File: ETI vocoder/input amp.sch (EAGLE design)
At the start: 32 parts, among them IC1 LM4558N, IC2 LM1458N

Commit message: Fixed input boards in regards to article and added spacer holes
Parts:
- C4: device resistor:C-EU050-025X075 -> resistor:C-EU025-025X050
- R8: value (none) -> 47k
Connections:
- net N$10: now also RV2G$1.1E; no longer RV2G$1.1A
- net N$9: now also RV2G$1.1A; no longer RV2G$1.1E
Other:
- note added: "Har sjekket footprint caps"
- note added: "Har sjekket retning på pots!"
- note removed: "Sjekk retning på pots!"
- moved on the sheet: RV2
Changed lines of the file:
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@@
 <?xml version="1.0" encoding="utf-8"?>
 <!DOCTYPE eagle SYSTEM "eagle.dtd">
-<eagle version="7.2.0">
+<eagle version="6.2">
 <drawing>
 <settings>
@@
 <layers>
 <layer number="1" name="Top" color="4" fill="1" visible="no" active="no"/>
+<layer number="2" name="Route2" color="1" fill="3" visible="no" active="no"/>
+<layer number="3" name="Route3" color="4" fill="3" visible="no" active="no"/>
+<layer number="14" name="Route14" color="1" fill="6" visible="no" active="no"/>
+<layer number="15" name="Route15" color="4" fill="6" visible="no" active="no"/>
 <layer number="16" name="Bottom" color="1" fill="1" visible="no" active="no"/>
 <layer number="17" name="Pads" color="2" fill="1" visible="no" active="no"/>
@@
 <part name="R6" library="resistor" deviceset="R-EU_" device="0207/7" value="1k5"/>
 <part name="R7" library="resistor" deviceset="R-EU_" device="0207/7" value="51k"/>
-<part name="R8" library="resistor" deviceset="R-EU_" device="0207/7"/>
+<part name="R8" library="resistor" deviceset="R-EU_" device="0207/7" value="47k"/>
 <part name="R9" library="resistor" deviceset="R-EU_" device="0207/7" value="51k"/>
 <part name="R10" library="resistor" deviceset="R-EU_" device="0207/7" value="47k"/>
@@
 <part name="C2" library="resistor" deviceset="CPOL-EU" device="E2.5-5" value="22u"/>
 <part name="C3" library="resistor" deviceset="C-EU" device="050-025X075" value="220n"/>
-<part name="C4" library="resistor" deviceset="C-EU" device="050-025X075" value="68p"/>
+<part name="C4" library="resistor" deviceset="C-EU" device="025-025X050" value="68p"/>
 <part name="C5" library="resistor" deviceset="C-EU" device="050-025X075" value="2n2"/>
 <part name="C6" library="resistor" deviceset="C-EU" device="050-025X075" value="2n2"/>
@@
 <sheet>
 <plain>
-<text x="-12.7" y="101.6" size="1.778" layer="91">Sjekk retning på pots!</text>
+<text x="-12.7" y="101.6" size="1.778" layer="91">Har sjekket retning på pots!</text>
+<text x="-12.7" y="96.52" size="1.778" layer="91">Har sjekket footprint caps</text>
 </plain>
 <instances>
@@
 </instance>
 <instance part="GND3" gate="1" x="66.04" y="50.8"/>
-<instance part="RV2" gate="G$1" x="88.9" y="63.5" smashed="yes" rot="R90">
-<attribute name="NAME" x="85.344" y="59.436" size="1.778" layer="95" rot="R90"/>
+<instance part="RV2" gate="G$1" x="88.9" y="63.5" smashed="yes" rot="MR270">
+<attribute name="NAME" x="85.344" y="67.564" size="1.778" layer="95" rot="MR270"/>
 </instance>
 <instance part="GND4" gate="1" x="101.6" y="55.88"/>
@@
 <label x="66.04" y="33.02" size="1.778" layer="95"/>
 <junction x="66.04" y="22.86"/>
+<junction x="66.04" y="33.02"/>
 </segment>
 <segment>
@@
 <wire x1="73.66" y1="71.12" x2="96.52" y2="71.12" width="0.1524" layer="91"/>
 <wire x1="96.52" y1="71.12" x2="96.52" y2="68.58" width="0.1524" layer="91"/>
-<pinref part="RV2" gate="G$1" pin="1E"/>
-<wire x1="96.52" y1="68.58" x2="93.98" y2="68.58" width="0.1524" layer="91"/>
 <pinref part="C6" gate="G$1" pin="1"/>
 <junction x="96.52" y="71.12"/>
+<pinref part="RV2" gate="G$1" pin="1A"/>
+<wire x1="93.98" y1="68.58" x2="96.52" y2="68.58" width="0.1524" layer="91"/>
 </segment>
 </net>
 <net name="N$10" class="0">
 <segment>
-<pinref part="RV2" gate="G$1" pin="1A"/>
-<pinref part="C5" gate="G$1" pin="2"/>
-<wire x1="93.98" y1="58.42" x2="99.06" y2="58.42" width="0.1524" layer="91"/>
 <wire x1="99.06" y1="58.42" x2="99.06" y2="48.26" width="0.1524" layer="91"/>
 <pinref part="R10" gate="G$1" pin="1"/>
 <wire x1="99.06" y1="48.26" x2="104.14" y2="48.26" width="0.1524" layer="91"/>
+<pinref part="C5" gate="G$1" pin="2"/>
+<pinref part="RV2" gate="G$1" pin="1E"/>
+<wire x1="99.06" y1="58.42" x2="93.98" y2="58.42" width="0.1524" layer="91"/>
 <junction x="93.98" y="58.42"/>
 </segment>
@@
 <pinref part="C5" gate="G$1" pin="1"/>
 <pinref part="R7" gate="G$1" pin="2"/>
-</segment>
-</net>
-<net name="N$12" class="0">
-<segment>
-<pinref part="RV2" gate="G$1" pin="1S"/>
-<pinref part="IC2" gate="A" pin="+IN"/>
-<wire x1="93.98" y1="63.5" x2="104.14" y2="63.5" width="0.1524" layer="91"/>
 </segment>
 </net>
@@
 </segment>
 </net>
+<net name="N$3" class="0">
+<segment>
+<pinref part="RV2" gate="G$1" pin="1S"/>
+<pinref part="IC2" gate="A" pin="+IN"/>
+<wire x1="93.98" y1="63.5" x2="104.14" y2="63.5" width="0.1524" layer="91"/>
+</segment>
+</net>

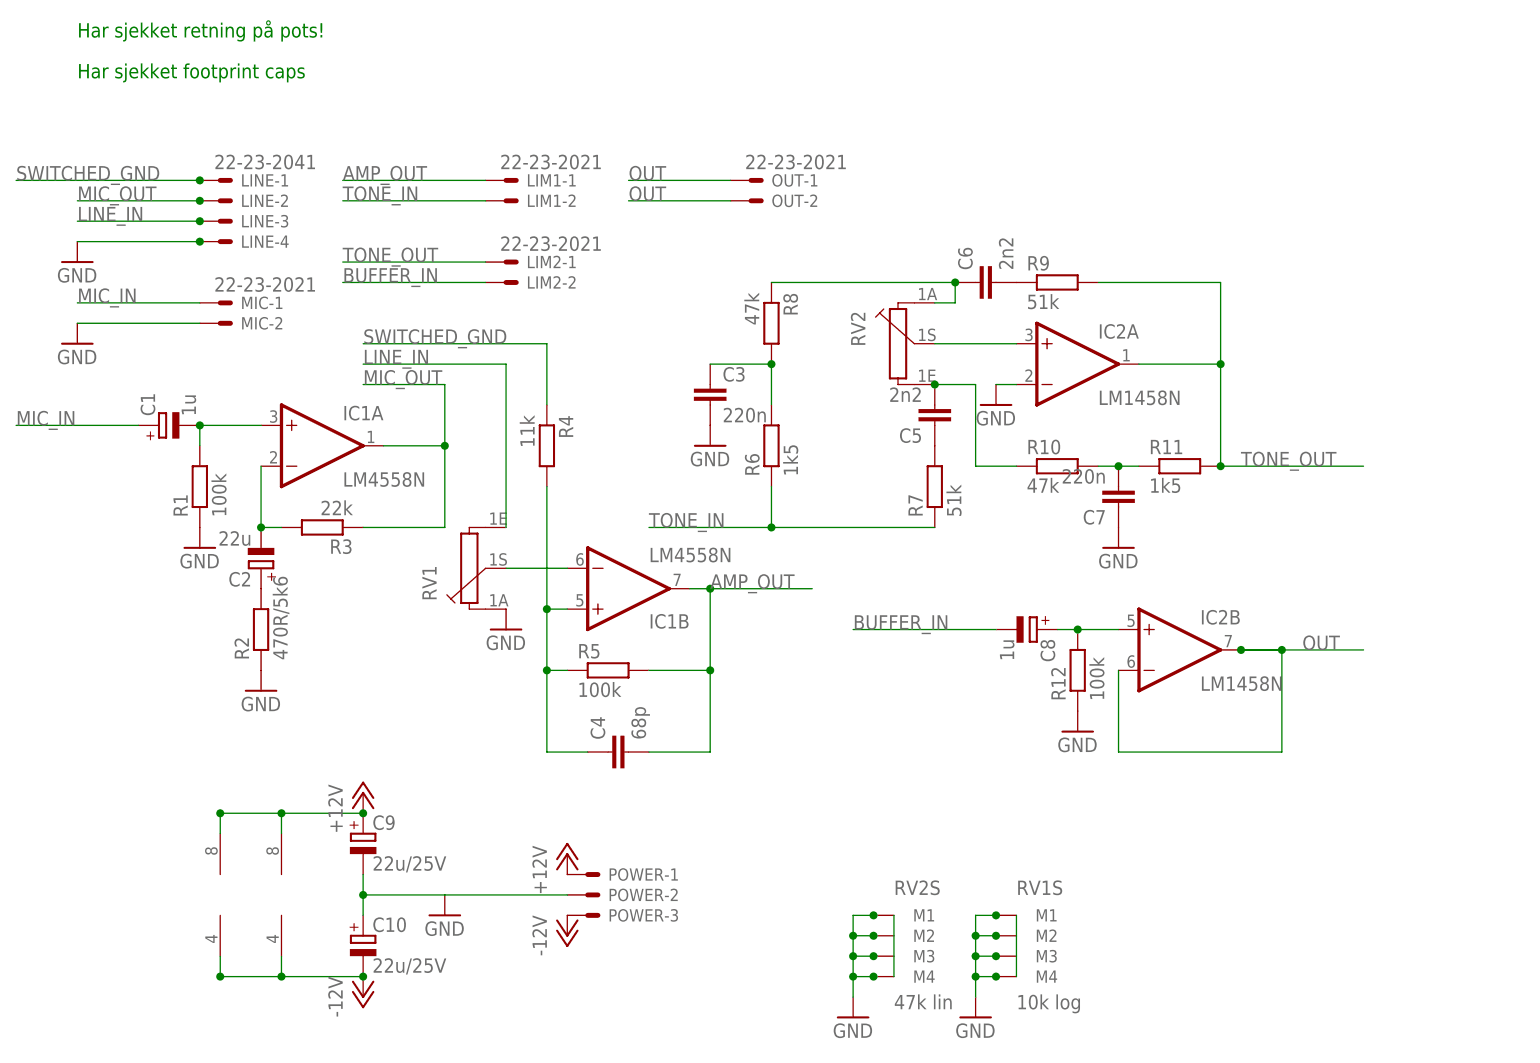
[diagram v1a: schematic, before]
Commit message: Finished first of two halves of the universal voice board
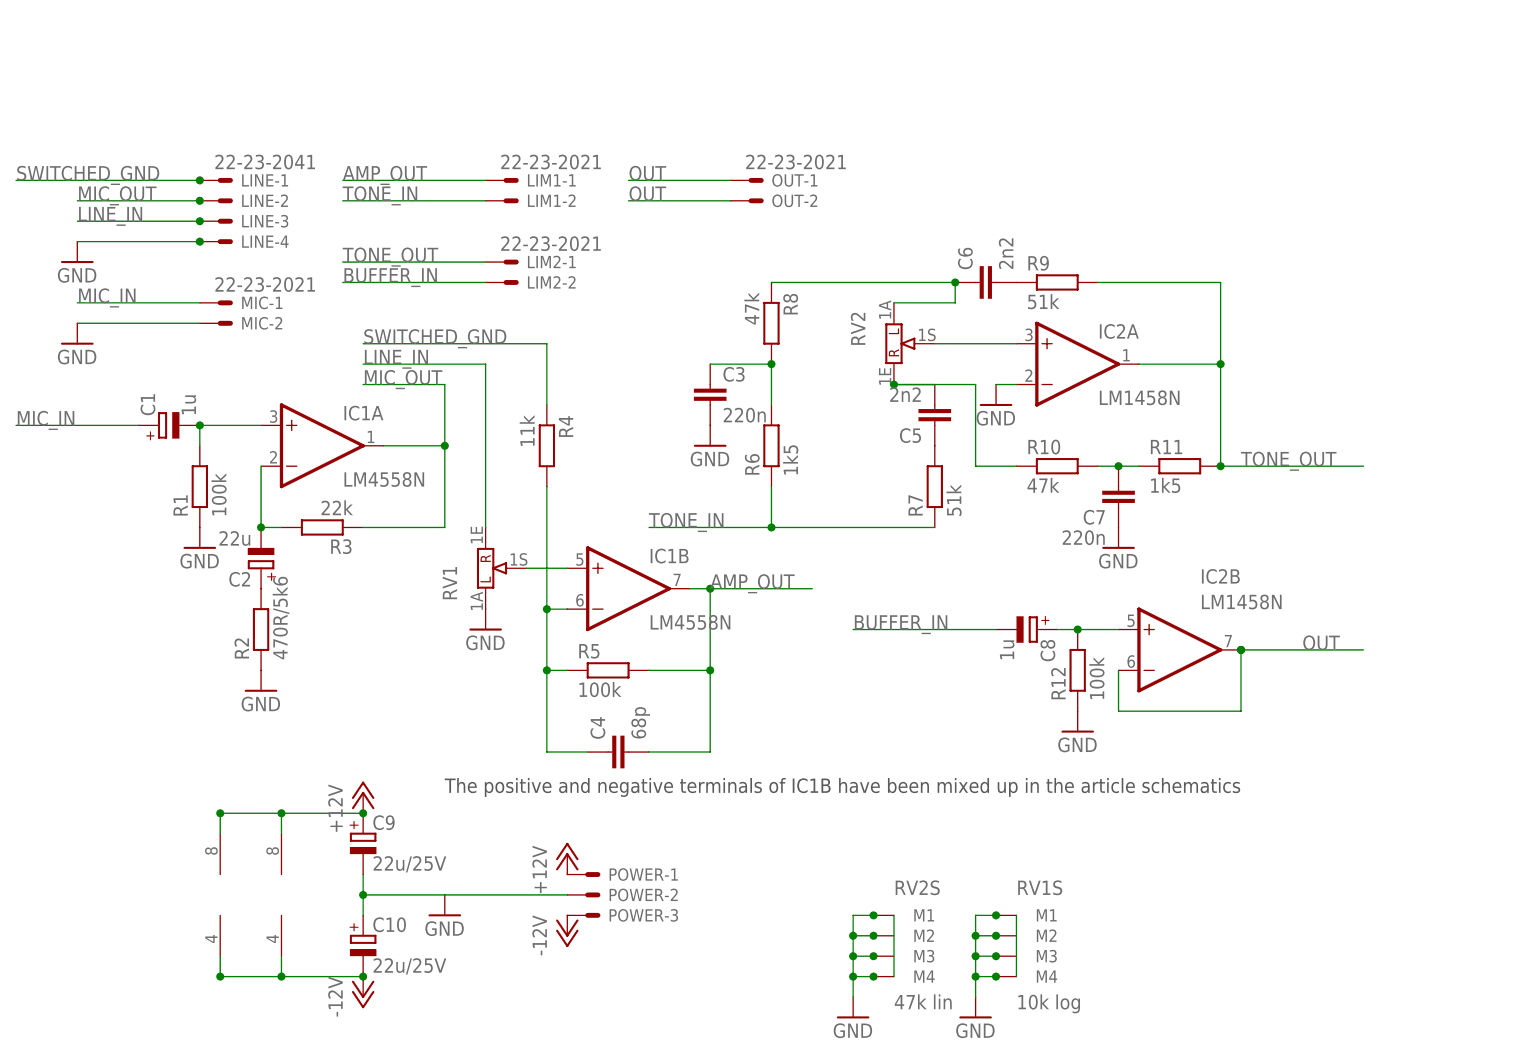
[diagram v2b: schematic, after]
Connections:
- net N$5: now also IC1B.+IN; no longer IC1B.-IN
- net N$6: now also IC1B.-IN; no longer IC1B.+IN
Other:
- note added: "The positive and negative terminals of IC1B have been mixed up in the article schematics"
- note removed: "Har sjekket footprint caps"
- note removed: "Har sjekket retning på pots!"
- moved on the sheet: IC1B
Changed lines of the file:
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@@
 <sheet>
 <plain>
-<text x="-12.7" y="101.6" size="1.778" layer="91">Har sjekket retning på pots!</text>
-<text x="-12.7" y="96.52" size="1.778" layer="91">Har sjekket footprint caps</text>
+<text x="33.02" y="7.62" size="1.778" layer="97">The positive and negative terminals of IC1B have been mixed up in the article schematics</text>
 </plain>
 <instances>
 <instance part="IC1" gate="A" x="17.78" y="50.8"/>
-<instance part="IC1" gate="B" x="55.88" y="33.02" rot="MR180"/>
+<instance part="IC1" gate="B" x="55.88" y="33.02"/>
 <instance part="IC1" gate="P" x="12.7" y="-5.08"/>
 <instance part="IC2" gate="A" x="111.76" y="60.96"/>
-<instance part="IC2" gate="B" x="124.46" y="25.4"/>
+<instance part="IC2" gate="B" x="124.46" y="25.4" smashed="yes">
+<attribute name="NAME" x="127" y="33.655" size="1.778" layer="95"/>
+<attribute name="VALUE" x="127" y="30.48" size="1.778" layer="96"/>
+</instance>
 <instance part="R1" gate="G$1" x="2.54" y="45.72" rot="R90"/>
 <instance part="R2" gate="G$1" x="10.16" y="27.94" rot="R90"/>
@@
 <instance part="C5" gate="G$1" x="93.98" y="53.34" rot="R180"/>
 <instance part="C6" gate="G$1" x="99.06" y="71.12" rot="R90"/>
-<instance part="C7" gate="G$1" x="116.84" y="43.18" rot="R180"/>
+<instance part="C7" gate="G$1" x="116.84" y="43.18" smashed="yes" rot="R180">
+<attribute name="NAME" x="115.316" y="42.799" size="1.778" layer="95" rot="R180"/>
+<attribute name="VALUE" x="115.316" y="40.259" size="1.778" layer="96" rot="R180"/>
+</instance>
 <instance part="C8" gate="G$1" x="106.68" y="27.94" rot="R270"/>
 <instance part="C9" gate="G$1" x="22.86" y="2.54"/>
@@
 <instance part="GND1" gate="1" x="2.54" y="38.1"/>
 <instance part="GND2" gate="1" x="10.16" y="20.32"/>
-<instance part="RV1" gate="G$1" x="35.56" y="35.56" smashed="yes" rot="R90">
-<attribute name="NAME" x="32.004" y="31.496" size="1.778" layer="95" rot="R90"/>
+<instance part="RV1" gate="G$1" x="38.1" y="35.56" smashed="yes" rot="R90">
+<attribute name="NAME" x="34.544" y="31.496" size="1.778" layer="95" rot="R90"/>
 </instance>
 <instance part="GND3" gate="1" x="66.04" y="50.8"/>
@@
 <instance part="GND5" gate="1" x="116.84" y="38.1"/>
 <instance part="GND6" gate="1" x="111.76" y="15.24"/>
-<instance part="GND7" gate="1" x="40.64" y="27.94"/>
+<instance part="GND7" gate="1" x="38.1" y="27.94"/>
 <instance part="GND8" gate="1" x="33.02" y="-7.62"/>
 <instance part="P+1" gate="1" x="22.86" y="7.62"/>
@@
 </segment>
 </net>
-<net name="N$5" class="0">
-<segment>
-<pinref part="RV1" gate="G$1" pin="1S"/>
-<pinref part="IC1" gate="B" pin="-IN"/>
-<wire x1="40.64" y1="35.56" x2="48.26" y2="35.56" width="0.1524" layer="91"/>
-</segment>
-</net>
 <net name="N$6" class="0">
 <segment>
-<pinref part="IC1" gate="B" pin="+IN"/>
-<wire x1="45.72" y1="30.48" x2="48.26" y2="30.48" width="0.1524" layer="91"/>
-<wire x1="45.72" y1="30.48" x2="45.72" y2="22.86" width="0.1524" layer="91"/>
 <pinref part="C4" gate="G$1" pin="1"/>
 <wire x1="45.72" y1="22.86" x2="45.72" y2="12.7" width="0.1524" layer="91"/>
@@
 <junction x="45.72" y="22.86"/>
 <pinref part="R4" gate="G$1" pin="2"/>
+<wire x1="45.72" y1="22.86" x2="45.72" y2="30.48" width="0.1524" layer="91"/>
+<pinref part="IC1" gate="B" pin="-IN"/>
 <wire x1="45.72" y1="30.48" x2="45.72" y2="45.72" width="0.1524" layer="91"/>
+<wire x1="48.26" y1="30.48" x2="45.72" y2="30.48" width="0.1524" layer="91"/>
 <junction x="45.72" y="30.48"/>
 </segment>
@@
 <junction x="96.52" y="71.12"/>
 <pinref part="RV2" gate="G$1" pin="1A"/>
-<wire x1="93.98" y1="68.58" x2="96.52" y2="68.58" width="0.1524" layer="91"/>
+<wire x1="88.9" y1="68.58" x2="96.52" y2="68.58" width="0.1524" layer="91"/>
 </segment>
 </net>
@@
 <pinref part="C5" gate="G$1" pin="2"/>
 <pinref part="RV2" gate="G$1" pin="1E"/>
-<wire x1="99.06" y1="58.42" x2="93.98" y2="58.42" width="0.1524" layer="91"/>
-<junction x="93.98" y="58.42"/>
+<wire x1="99.06" y1="58.42" x2="88.9" y2="58.42" width="0.1524" layer="91"/>
+<junction x="88.9" y="58.42"/>
+<wire x1="93.98" y1="58.42" x2="88.9" y2="58.42" width="0.1524" layer="91"/>
 </segment>
 </net>
@@
 <segment>
 <pinref part="IC2" gate="B" pin="-IN"/>
-<wire x1="116.84" y1="22.86" x2="116.84" y2="12.7" width="0.1524" layer="91"/>
-<wire x1="116.84" y1="12.7" x2="137.16" y2="12.7" width="0.1524" layer="91"/>
-<wire x1="137.16" y1="12.7" x2="137.16" y2="25.4" width="0.1524" layer="91"/>
+<wire x1="116.84" y1="22.86" x2="116.84" y2="17.78" width="0.1524" layer="91"/>
+<wire x1="116.84" y1="17.78" x2="132.08" y2="17.78" width="0.1524" layer="91"/>
+<wire x1="132.08" y1="17.78" x2="132.08" y2="25.4" width="0.1524" layer="91"/>
 <pinref part="IC2" gate="B" pin="OUT"/>
-<wire x1="137.16" y1="25.4" x2="132.08" y2="25.4" width="0.1524" layer="91"/>
-<wire x1="132.08" y1="25.4" x2="137.16" y2="25.4" width="0.1524" layer="91"/>
 <label x="139.7" y="25.4" size="1.778" layer="95"/>
-<junction x="137.16" y="25.4"/>
-<wire x1="137.16" y1="25.4" x2="147.32" y2="25.4" width="0.1524" layer="91"/>
+<junction x="132.08" y="25.4"/>
+<wire x1="132.08" y1="25.4" x2="147.32" y2="25.4" width="0.1524" layer="91"/>
 <junction x="132.08" y="25.4"/>
 </segment>
@@
 <segment>
 <pinref part="RV1" gate="G$1" pin="1E"/>
-<wire x1="40.64" y1="40.64" x2="40.64" y2="60.96" width="0.1524" layer="91"/>
-<wire x1="40.64" y1="60.96" x2="22.86" y2="60.96" width="0.1524" layer="91"/>
+<wire x1="38.1" y1="40.64" x2="38.1" y2="60.96" width="0.1524" layer="91"/>
+<wire x1="38.1" y1="60.96" x2="22.86" y2="60.96" width="0.1524" layer="91"/>
 <label x="22.86" y="60.96" size="1.778" layer="95"/>
 </segment>
@@
 </segment>
 </net>
+<net name="N$5" class="0">
+<segment>
+<pinref part="RV1" gate="G$1" pin="1S"/>
+<pinref part="IC1" gate="B" pin="+IN"/>
+<wire x1="43.18" y1="35.56" x2="48.26" y2="35.56" width="0.1524" layer="91"/>
+</segment>
+</net>
